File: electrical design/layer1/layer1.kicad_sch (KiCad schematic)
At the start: 95 parts, among them J1 Conn_01x08_Male, J2 Conn_01x06_Female, J3 Conn_01x03_Female, SW1 SW_DPDT_x2, SW2 SW_DPDT_x2, SW3 SW_Push, U1 STM32F103C8T6, U2 CD74HC4067SM, U3 CD74HC4067SM, Y1 Crystal

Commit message: rename files
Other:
- company: 8076 robotics -> 8076 Robotics
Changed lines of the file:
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@@
     (date "2022-12-02")
     (rev "v0.2")
-    (company "8076 robotics")
+    (company "8076 Robotics")
   )
   (junction (at 165.1 25.4) (diameter 0) (color 0 0 0 0)

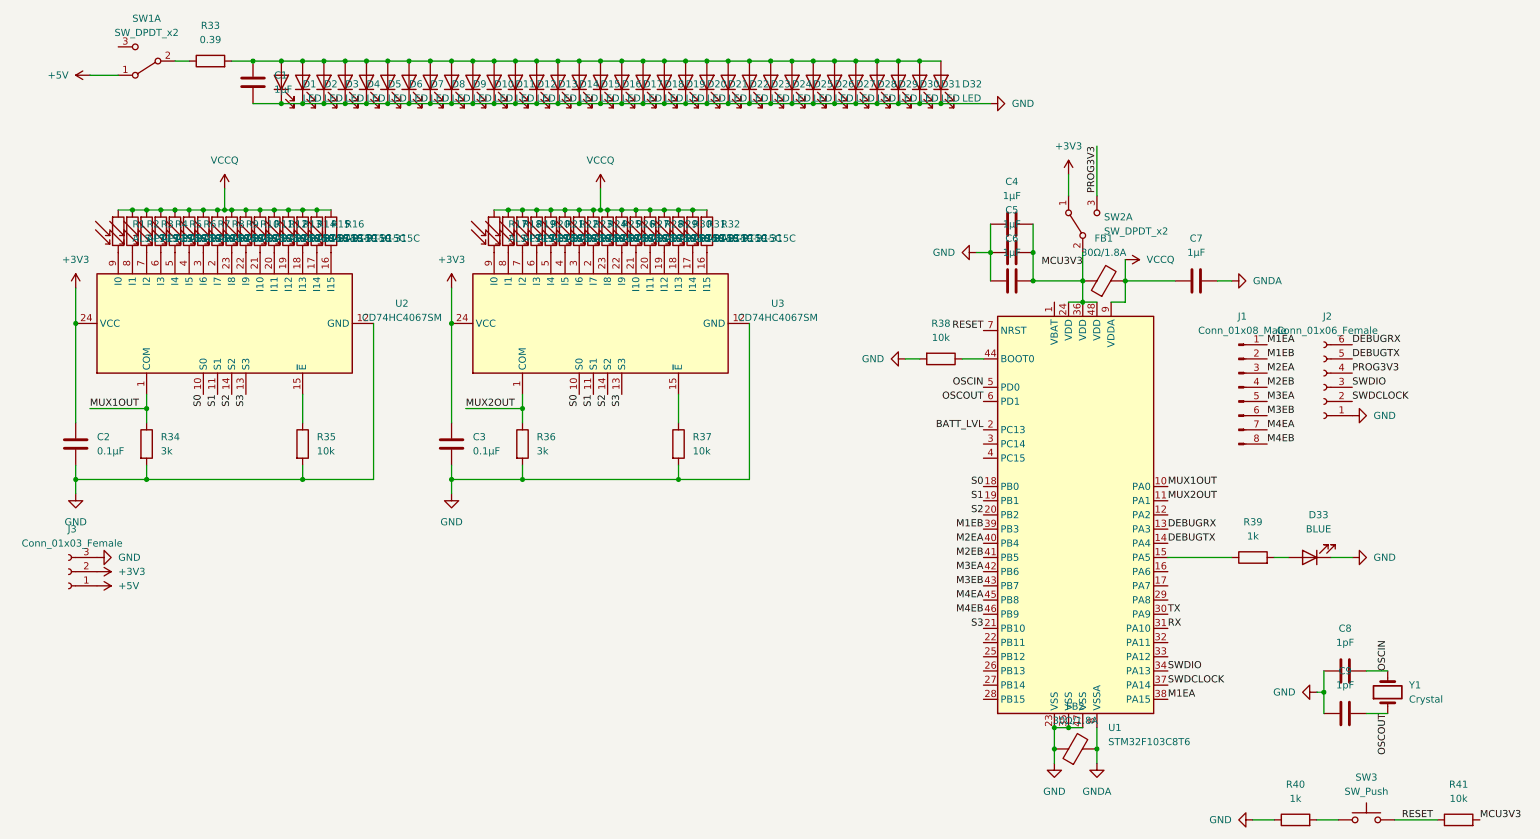
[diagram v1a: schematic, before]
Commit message: update layer 1 and 3 schematics
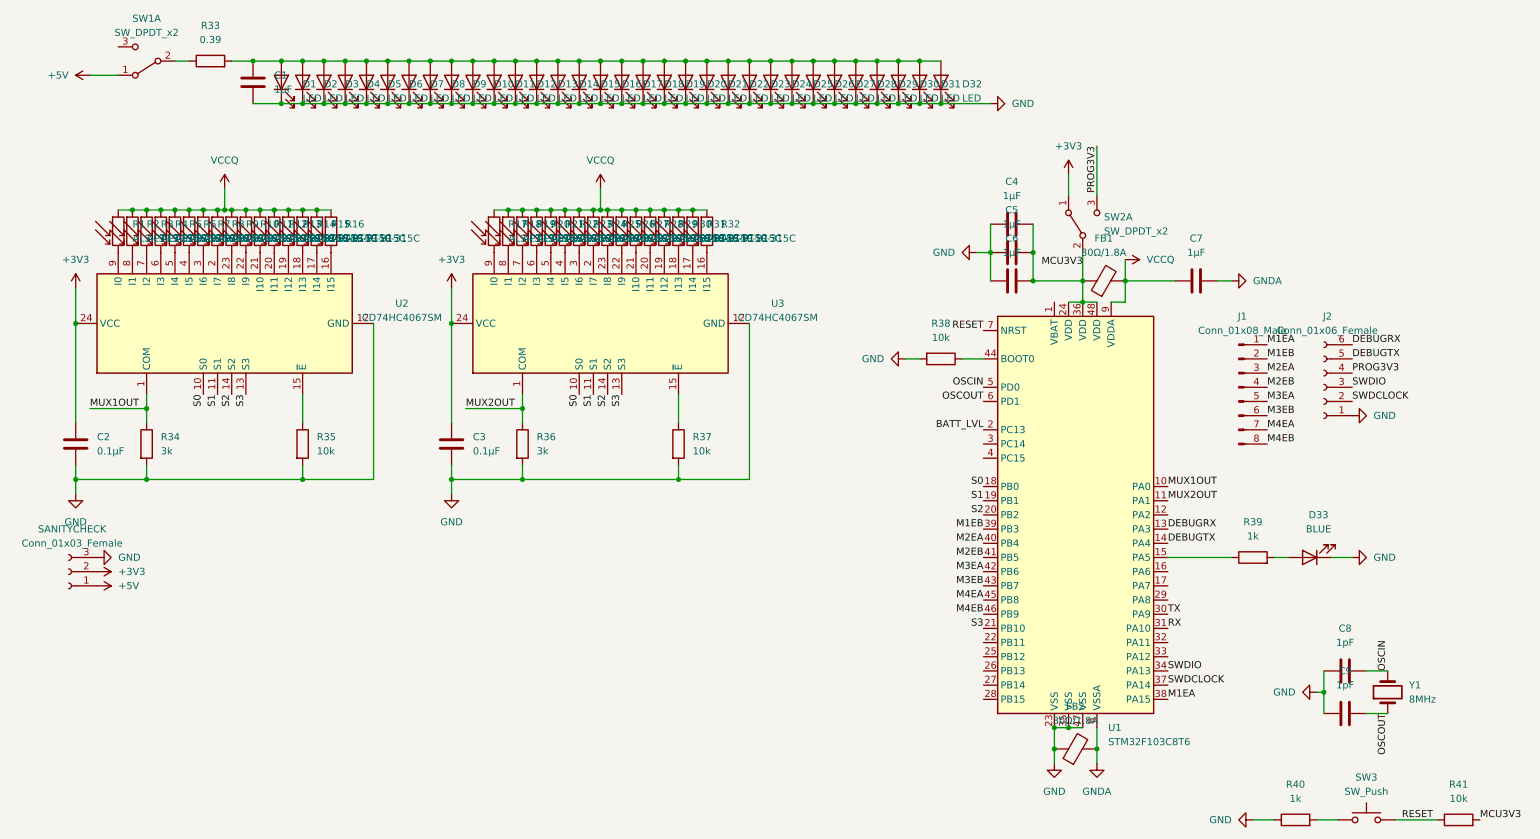
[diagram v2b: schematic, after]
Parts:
- Y1: value Crystal -> 8MHz
- renumbered J3 to SANITYCHECK
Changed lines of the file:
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@@
       (effects (font (size 1.27 1.27)) (justify right))
     )
-    (property "Value" "Crystal" (id 1) (at 260.35 139.6999 90)
+    (property "Value" "8MHz" (id 1) (at 260.35 139.6999 90)
       (effects (font (size 1.27 1.27)) (justify right))
     )
@@
   (symbol (lib_id "Connector:Conn_01x03_Female") (at 20.32 116.84 180) (unit 1)
     (in_bom yes) (on_board yes) (fields_autoplaced)
-    (property "Reference" "J3" (id 0) (at 20.955 109.22 0))
+    (property "Reference" "SANITYCHECK" (id 0) (at 20.955 109.22 0))
     (property "Value" "Conn_01x03_Female" (id 1) (at 20.955 111.76 0))
     (property "Footprint" "" (id 2) (at 20.32 116.84 0)
@@
       (reference "J2") (unit 1) (value "Conn_01x06_Female") (footprint "Connector_JST:JST_SH_BM06B-SRSS-TB_1x06-1MP_P1.00mm_Vertical")
     )
-    (path "/86937535-1a00-4375-a966-feffacfd480e"
-      (reference "J3") (unit 1) (value "Conn_01x03_Female") (footprint "")
-    )
     (path "/fa77eeda-ce5b-40dc-b111-3164550acfac"
       (reference "R1") (unit 1) (value "ALS-PT19-315C") (footprint "")
@@
       (reference "R41") (unit 1) (value "10k") (footprint "")
     )
+    (path "/86937535-1a00-4375-a966-feffacfd480e"
+      (reference "SANITYCHECK") (unit 1) (value "Conn_01x03_Female") (footprint "")
+    )
     (path "/f3aee012-2aae-4ec5-a907-35ecf6a2255c"
       (reference "SW1") (unit 1) (value "SW_DPDT_x2") (footprint "")
@@
     )
     (path "/1dfbef3b-0871-4e82-bc53-1e2b60a4ef56"
-      (reference "Y1") (unit 1) (value "Crystal") (footprint "Clocks:CRYSTAL-SMD-5X3.2-2PAD")
-    )
-  )
+      (reference "Y1") (unit 1) (value "8MHz") (footprint "Clocks:CRYSTAL-SMD-5X3.2-2PAD")
+    )
+  )
